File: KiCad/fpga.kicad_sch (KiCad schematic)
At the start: 0 parts

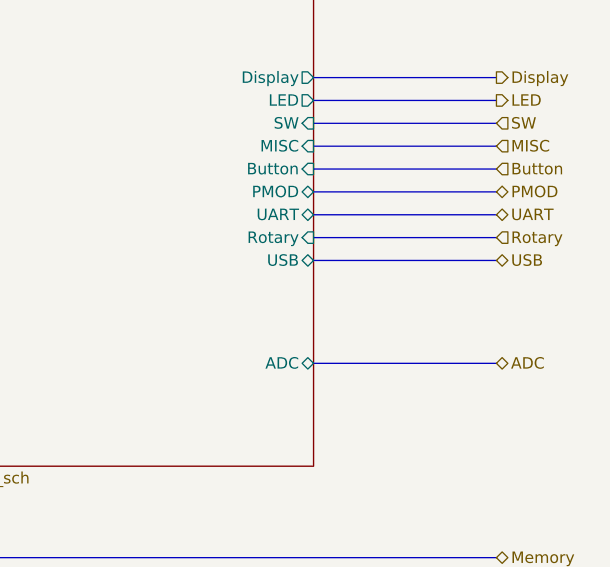
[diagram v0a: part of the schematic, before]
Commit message: micro-SD hinzugefügt
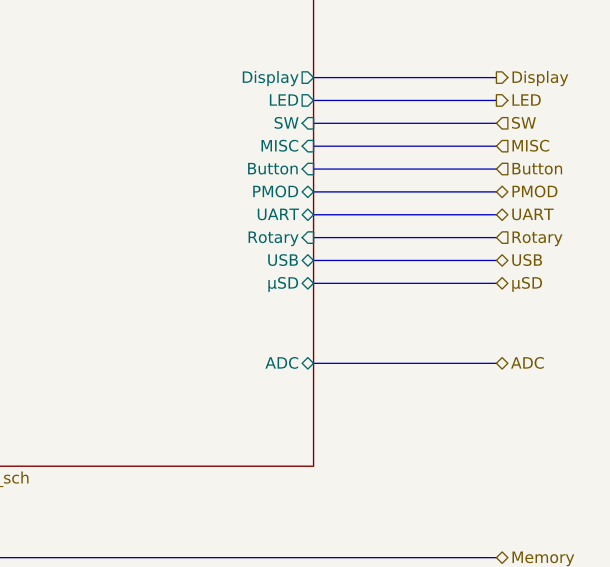
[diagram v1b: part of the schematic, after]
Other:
- sheet FPGA_IO ports: added μSD; removed none
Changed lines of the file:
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@@
+	(bus
+		(pts
+			(xy 196.85 86.36) (xy 217.17 86.36)
+		)
+		(stroke
+			(width 0)
+			(type default)
+		)
+	)
 	(bus
 		(pts
@@
 		(shape input)
 		(at 217.17 73.66 0)
+		(effects
+			(font
+				(size 1.27 1.27)
+			)
+			(justify left)
+		)
+	)
+	(hierarchical_label "μSD"
+		(shape bidirectional)
+		(at 217.17 86.36 0)
 		(effects
 			(font
@@
 			)
 		)
+		(pin "μSD" bidirectional
+			(at 196.85 86.36 0)
+			(effects
+				(font
+					(size 1.27 1.27)
+				)
+				(justify right)
+			)
+		)
